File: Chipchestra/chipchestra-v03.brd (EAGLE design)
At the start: 100 x 80 mm, 41 parts, among them IC1 OPA2134PA, U1 JOYSTICKPTH, U2 JOYSTICKPTH

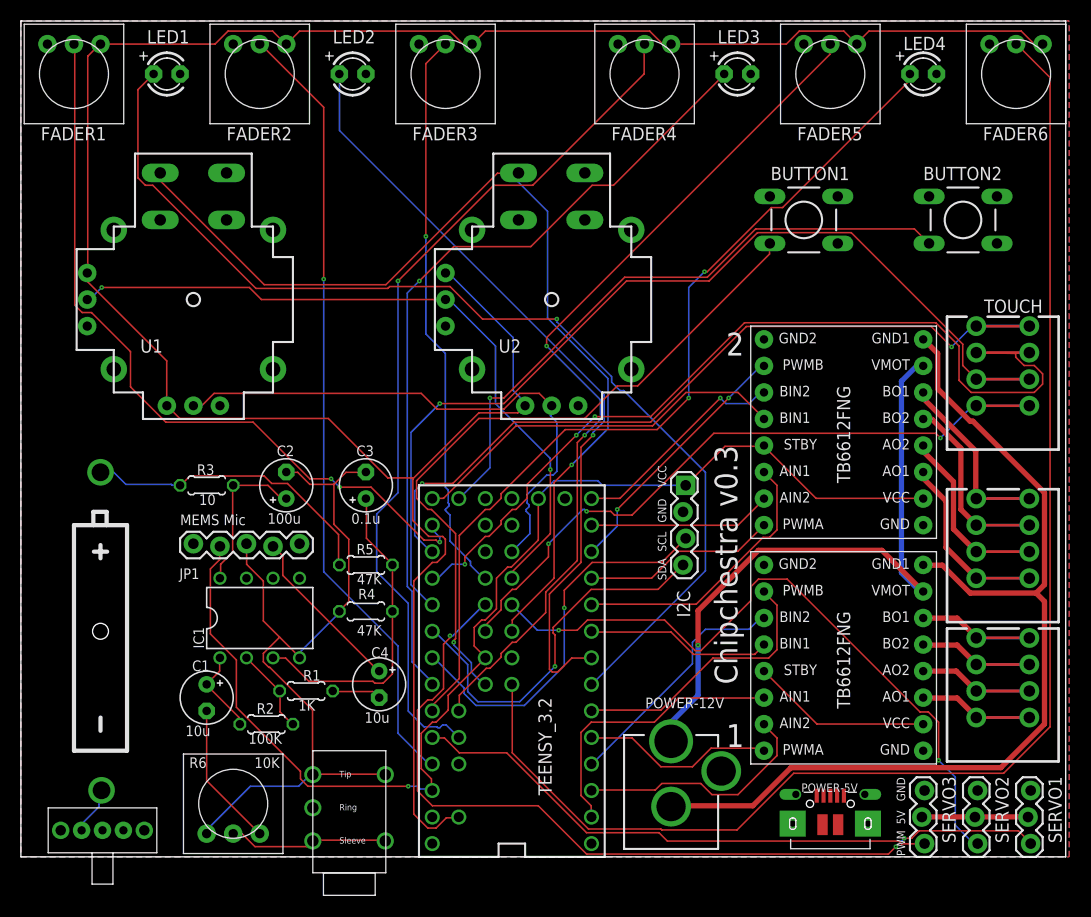
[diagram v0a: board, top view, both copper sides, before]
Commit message: new mic preamps added
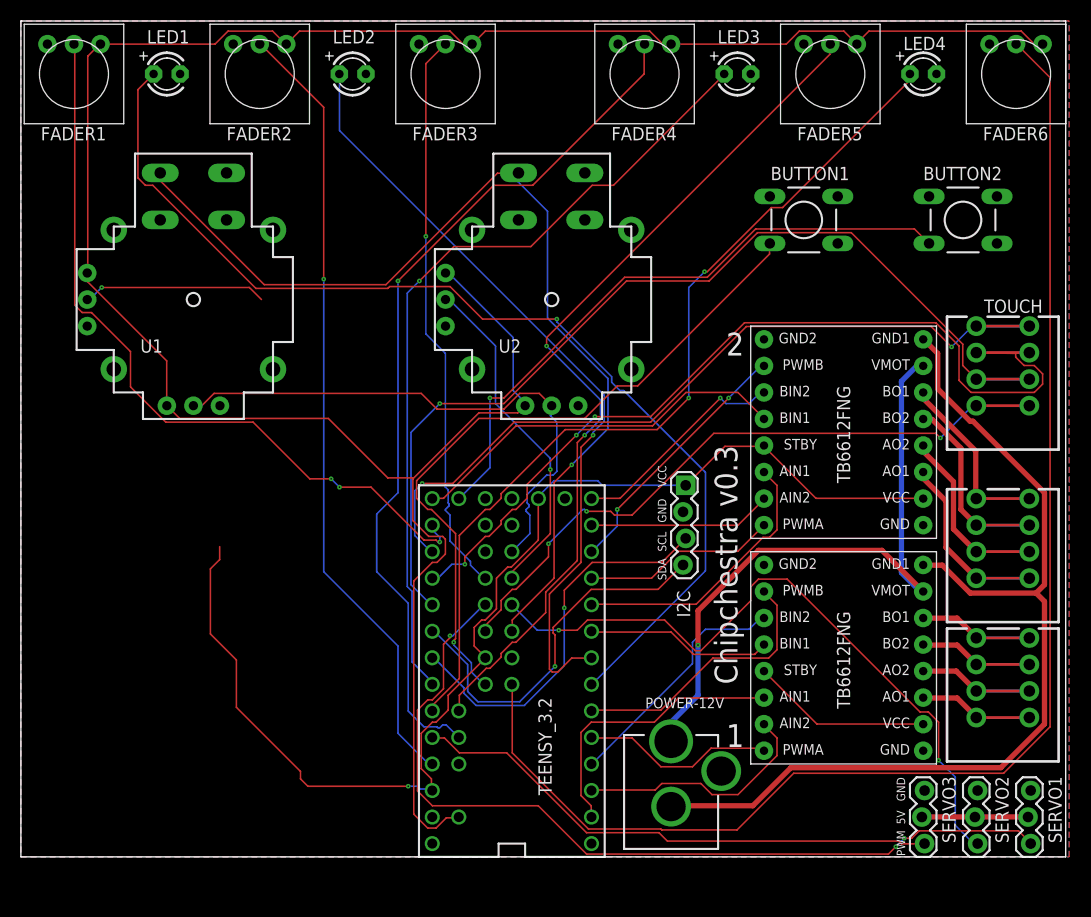
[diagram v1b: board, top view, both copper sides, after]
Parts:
- removed BAT1: (no value), Daniel:BATTERY-A23
- removed C1, C4: 10u, rcl:E2,5-5
- removed C2: 100u, rcl:E2,5-5
- removed C3: 0.1u, rcl:E2,5-5
- removed IC1: OPA2134PA, linear:DIL08
- removed JP1: MEMS Mic, SparkFun-Connectors:1X05_LOCK
- removed ON/OFF: labl, Daniel:SPDT-SWITCH
- removed POWER-5V: (no value), microbuilder:4UCONN_20329
- removed R1: 1K, CMU-ArtFab:0204/5
- removed R2: 100K, CMU-ArtFab:0204/5
- removed R3: 10, CMU-ArtFab:0204/5
- removed R4, R5: 47K, CMU-ArtFab:0204/5
- removed R6: 10K, adafruit:TRIM-3386
- removed TO-AUDIO-IO: 1/8"-F-STEREO-PCB, CMU-ArtFab:1/8"-F-STEREO-PCB
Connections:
- removed net GND_MIC: C2.-, C3.-, IC1.4, JP1.3, R4.1, R6.1, TO-AUDIO-IO.TIP1, TO-AUDIO-IO.TIP2
- removed net N$1: C2.+, IC1.8, R3.1
- removed net N$13: ON/OFF.2
- removed net N$14: POWER-5V.VBUS
- removed net N$2: BAT1.GND@1, ON/OFF.1
- removed net N$3: C4.+, JP1.4
- removed net N$4: C4.-, R1.1
- removed net N$5: IC1.2, R1.2, R2.1
- removed net N$6: C1.-, R6.3
- removed net N$7: R6.2, TO-AUDIO-IO.SLEEVE1, TO-AUDIO-IO.SLEEVE2
- removed net N$8: C3.+, IC1.3, R4.2, R5.1
- removed net N$9: C1.+, IC1.1, R2.2
- removed net VMIC: BAT1.PWR@1, R3.2, R5.2
- net +3V3: no longer JP1.2
- net GND: no longer POWER-5V.BASE@1, POWER-5V.BASE@2, POWER-5V.GND, POWER-5V.SPRT@1, POWER-5V.SPRT@2, POWER-5V.SPRT@3, POWER-5V.SPRT@4
- net JOYB1: no longer U2.B1A
- net JOYB2: now also U2.B1A
- net JOYH1: no longer U2.H2
- net JOYH2: now also U2.H2
- net JOYV1: no longer U2.V2
- net JOYV2: now also U2.V2
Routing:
- net GND_MIC: track 76.3 -> 0.00 mm
- net N$8: track 30.6 -> 0.00 mm
- net VMIC: track 28.9 -> 0.00 mm
- net JOYV1: track 67.8 -> 49.9 mm
- net N$3: track 16.2 -> 0.00 mm
- net N$7: track 15.4 -> 0.00 mm
- net N$1: track 15.1 -> 0.00 mm
- net N$6: track 13.9 -> 0.00 mm
- net N$5: track 8.22 -> 0.00 mm
- net N$9: track 8.22 -> 0.00 mm
- net N$4: track 4.72 -> 0.00 mm
- net N$2: track 4.63 -> 0.00 mm
